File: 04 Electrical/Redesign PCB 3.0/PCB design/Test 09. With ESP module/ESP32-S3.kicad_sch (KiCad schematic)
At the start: 5 parts, among them U1 ESP32-S3-WROOM-1-N8R2

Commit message: Routing PCB test 9
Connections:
- net WS2812_CTRL is gone; now on net TOF_XSHUT: U1.39 (GPIO1/TOUCH1/ADC1_CH0)
- net Disp_CS: now also U1.7 (GPIO7/TOUCH7/ADC1_CH6); no longer U1.15 (GPIO3/TOUCH3/ADC1_CH2)
- net Disp_DC: now also U1.9 (GPIO16/U0CTS/ADC2_CH5/XTAL_32K_N); no longer U1.8 (GPIO15/U0RTS/ADC2_CH4/XTAL_32K_P)
- net Disp_LED: now also U1.15 (GPIO3/TOUCH3/ADC1_CH2); no longer U1.11 (GPIO18/U1RXD/ADC2_CH7/CLK_OUT3)
- net Disp_MISO: now also U1.21 (GPIO13/TOUCH13/ADC2_CH2/FSPIQ/FSPIIO7/SUBSPIQ); no longer U1.16 (GPIO46)
- net Disp_MOSI: now also U1.19 (GPIO11/TOUCH11/ADC2_CH0/FSPID/FSPIIO5/SUBSPID); no longer U1.18 (GPIO10/TOUCH10/ADC1_CH9/FSPICS0/FSPIIO4/SUBSPICS0)
- net Disp_RES: now also U1.8 (GPIO15/U0RTS/ADC2_CH4/XTAL_32K_P); no longer U1.7 (GPIO7/TOUCH7/ADC1_CH6)
- net Disp_SCK: now also U1.20 (GPIO12/TOUCH12/ADC2_CH1/FSPICLK/FSPIIO6/SUBSPICLK); no longer U1.17 (GPIO9/TOUCH9/ADC1_CH8/FSPIHD/SUBSPIHD)
- net SD_CS: now also U1.29 (SPIIO7/GPIO36/FSPICLK/SUBSPICLK); no longer U1.32 (MTCK/GPIO39/CLK_OUT3/SUBSPICS1)
- net SD_MISO: now also U1.31 (GPIO38/FSPIWP/SUBSPIWP); no longer U1.34 (MTDI/GPIO41/CLK_OUT1)
- net SD_MOSI: now also U1.30 (SPIDQS/GPIO37/FSPIQ/SUBSPIQ); no longer U1.33 (MTDO/GPIO40/CLK_OUT2)
- net SD_SCK: now also U1.32 (MTCK/GPIO39/CLK_OUT3/SUBSPICS1); no longer U1.35 (MTMS/GPIO42)
- net TOF_GPIO01: now also U1.38 (GPIO2/TOUCH2/ADC1_CH1); no longer U1.22 (GPIO14/TOUCH14/ADC2_CH3/FSPIWP/FSPIDQS/SUBSPIWP)
- net TOF_SCL: now also U1.37 (U0TXD/GPIO43/CLK_OUT1); no longer U1.20 (GPIO12/TOUCH12/ADC2_CH1/FSPICLK/FSPIIO6/SUBSPICLK)
- net TOF_SDA: now also U1.36 (U0RXD/GPIO44/CLK_OUT2); no longer U1.23 (GPIO21)
- net TOF_XSHUT: no longer U1.21 (GPIO13/TOUCH13/ADC2_CH2/FSPIQ/FSPIIO7/SUBSPIQ)
- net btn_back: now also U1.27 (GPIO0/BOOT); no longer U1.30 (SPIDQS/GPIO37/FSPIQ/SUBSPIQ)
- net btn_confirm: now also U1.28 (SPIIO6/GPIO35/FSPID/SUBSPID); no longer U1.31 (GPIO38/FSPIWP/SUBSPIWP)
- net btn_down: now also U1.33 (MTDO/GPIO40/CLK_OUT2); no longer U1.36 (U0RXD/GPIO44/CLK_OUT2)
- net btn_home: now also U1.35 (MTMS/GPIO42); no longer U1.38 (GPIO2/TOUCH2/ADC1_CH1)
- net btn_up: now also U1.34 (MTDI/GPIO41/CLK_OUT1); no longer U1.37 (U0TXD/GPIO43/CLK_OUT1)
- no-connect marks 10 -> 11

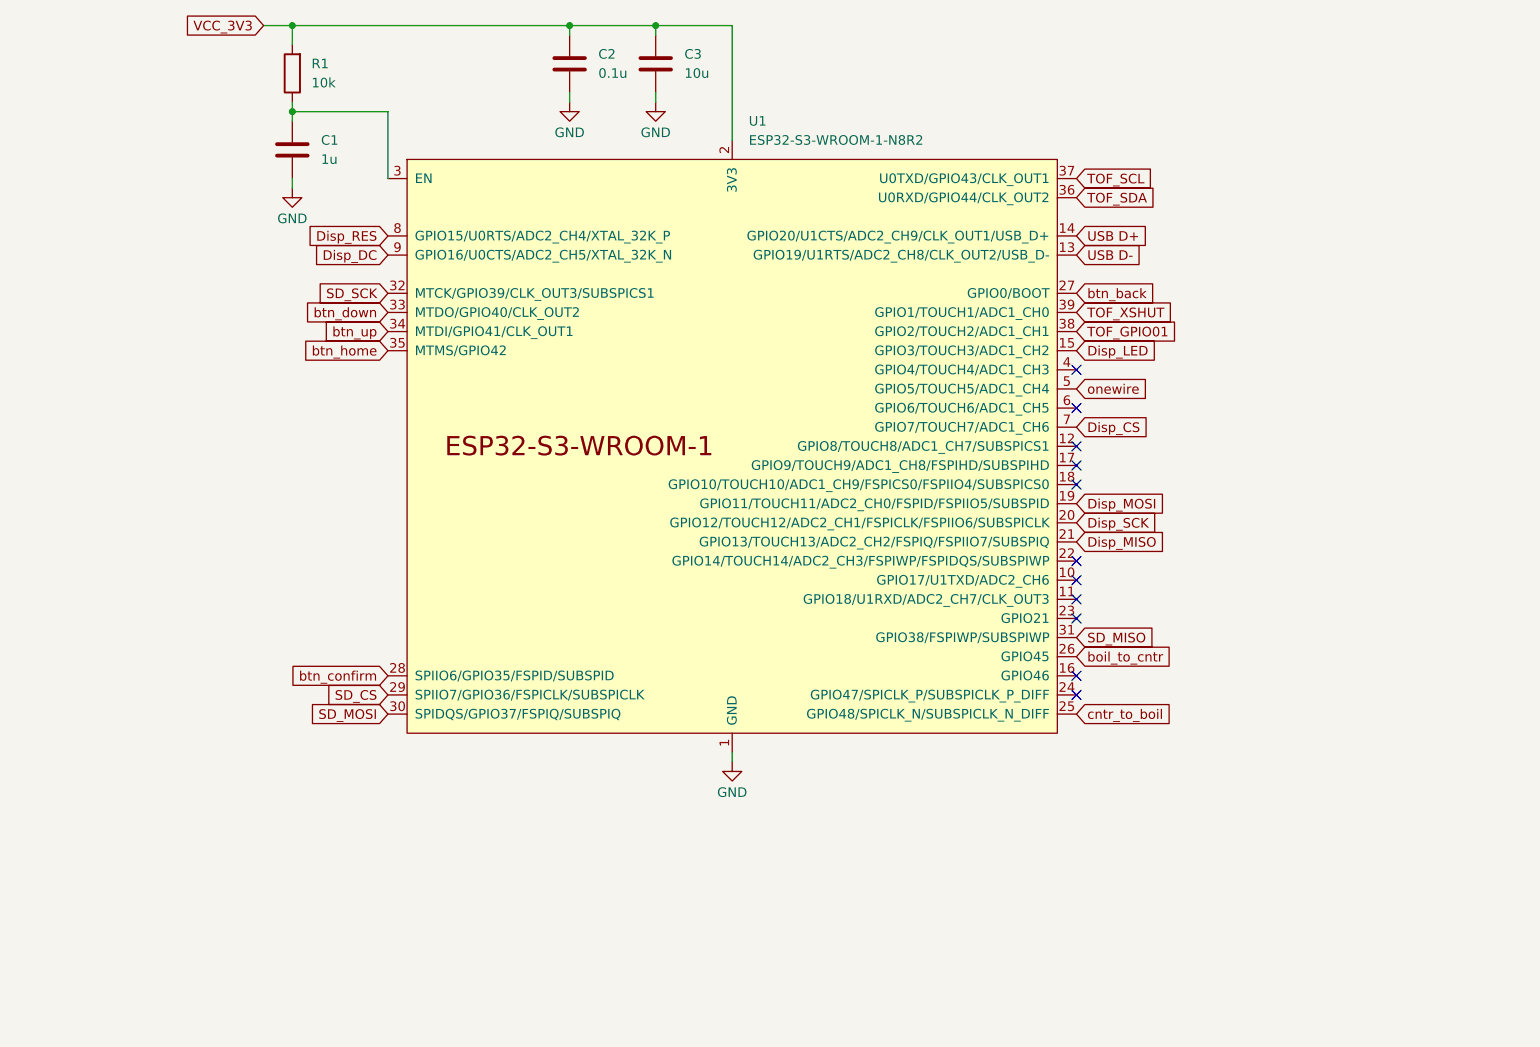
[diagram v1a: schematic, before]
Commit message: Logo added to PCB
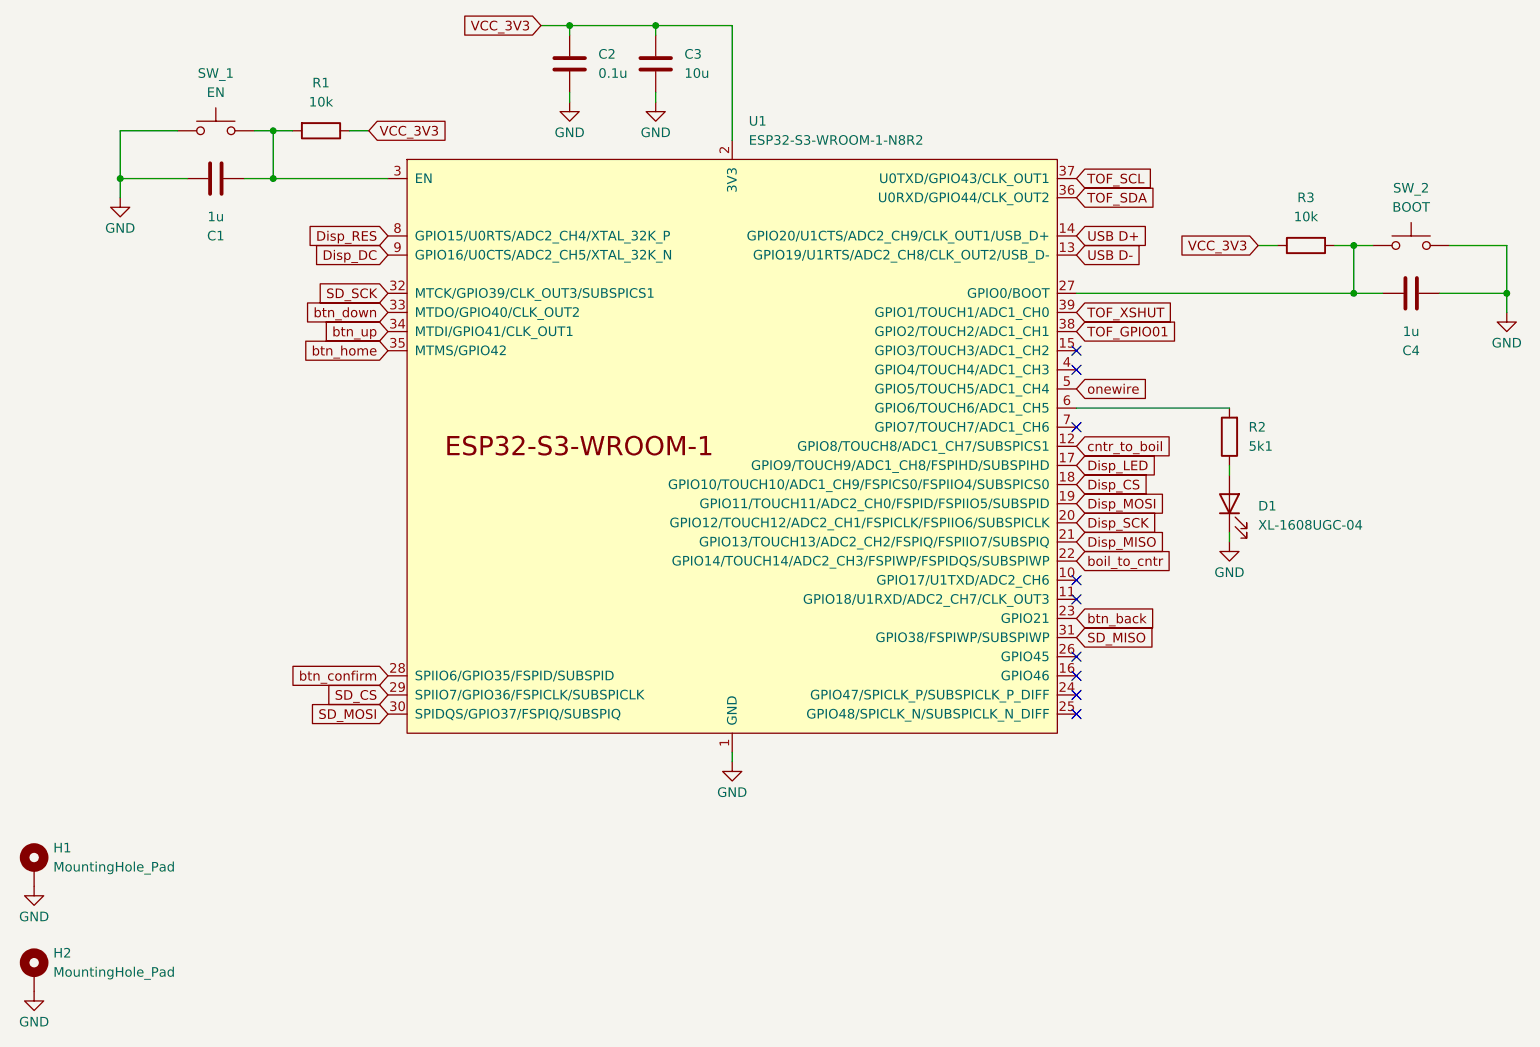
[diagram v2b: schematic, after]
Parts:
- added C4: 1u, Capacitor_SMD:C_0603_1608Metric, symbol Device:C
- added D1: XL-1608UGC-04, LED_SMD:LED_0603_1608Metric, symbol Device:LED
- added H1, H2: MountingHole_Pad, MountingHole:MountingHole_3.2mm_M3_ISO7380_Pad_TopBottom, symbol Mechanical:MountingHole_Pad
- added R2: 5k1, Resistor_SMD:R_0603_1608Metric, symbol Device:R
- added R3: 10k, Resistor_SMD:R_0603_1608Metric, symbol Device:R
- added SW_1: EN, Button_Switch_SMD:SW_SPST_TL3342, symbol Switch:SW_Push
- added SW_2: BOOT, Button_Switch_SMD:SW_SPST_TL3342, symbol Switch:SW_Push
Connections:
- net Disp_CS: now also U1.18 (GPIO10/TOUCH10/ADC1_CH9/FSPICS0/FSPIIO4/SUBSPICS0); no longer U1.7 (GPIO7/TOUCH7/ADC1_CH6)
- net Disp_LED: now also U1.17 (GPIO9/TOUCH9/ADC1_CH8/FSPIHD/SUBSPIHD); no longer U1.15 (GPIO3/TOUCH3/ADC1_CH2)
- net GND: now also C4.2, D1.1 (K), H1.1, H2.1, SW_1.2, SW_2.2
- net VCC_3V3: now also R1.1, R3.1; no longer R1.2
- net boil_to_cntr: now also U1.22 (GPIO14/TOUCH14/ADC2_CH3/FSPIWP/FSPIDQS/SUBSPIWP); no longer U1.26 (GPIO45)
- net btn_back: now also U1.23 (GPIO21); no longer U1.27 (GPIO0/BOOT)
- net cntr_to_boil: now also U1.12 (GPIO8/TOUCH8/ADC1_CH7/SUBSPICS1); no longer U1.25 (GPIO48/SPICLK_N/SUBSPICLK_N_DIFF)
- net at C1.1, U1.3 (EN): now also R1.2, SW_1.1; no longer R1.1
- net at U1.6 (GPIO6/TOUCH6/ADC1_CH5): now also R2.2
- new net: C4.1, R3.2, SW_2.1, U1.27 (GPIO0/BOOT)
- new net: D1.2 (A), R2.1
- no-connect marks 11 -> 9

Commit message: As ordered at JLCPCB
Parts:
- C3: LCSC Part #  C15525 -> C15525
- H1, H2: now not fitted
- SW_1, SW_2: LCSC C318884 -> (none); LCSC Part #  (none) -> C318884
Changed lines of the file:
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@@
 		(on_board yes)
 		(dnp no)
-		(property "Reference" "#PWR03"
+		(property "Reference" "#PWR05"
 			(at 140.97 57.15 0)
 			(effects
@@
 			(project "Test 09. With ESP module"
 				(path "/dee7d3c3-6abb-4cb3-8df4-3e3e37989a04/bd5268ae-2faf-441e-9d8c-8a98dae2e504"
-					(reference "#PWR03")
+					(reference "#PWR05")
 					(unit 1)
 				)
@@
 			)
 		)
+		(property "Comment" ""
+			(at 151.13 96.52 0)
+			(effects
+				(font
+					(size 1.27 1.27)
+				)
+				(hide yes)
+			)
+		)
 		(pin "16"
 		)
@@
 			)
 		)
-		(property "LCSC" "C318884"
+		(property "Comment" ""
+			(at 241.3 69.85 0)
+			(effects
+				(font
+					(size 1.27 1.27)
+				)
+				(hide yes)
+			)
+		)
+		(property "LCSC Part # " "C318884"
 			(at 241.3 69.85 0)
 			(effects
@@
 			)
 		)
-		(property "Datasheet" "~"
+		(property "Datasheet" "https://www.lcsc.com/datasheet/lcsc_datasheet_2206010045_UNI-ROYAL-Uniroyal-Elec-0603WAF1002T5E_C25804.pdf"
 			(at 227.33 69.85 0)
 			(effects
@@
 			)
 		)
-		(property "Description" "Resistor"
-			(at 227.33 69.85 0)
-			(effects
-				(font
-					(size 1.27 1.27)
-				)
-				(hide yes)
-			)
-		)
-		(property "Field7" ""
+		(property "Description" "100mW Thick Film Resistors 75V ±100ppm/℃ ±1% 10kΩ 0603 Chip Resistor - Surface Mount ROHS"
 			(at 227.33 69.85 0)
 			(effects
@@
 			)
 		)
+		(property "Comment" ""
+			(at 227.33 69.85 0)
+			(effects
+				(font
+					(size 1.27 1.27)
+				)
+				(hide yes)
+			)
+		)
 		(pin "2"
 		)
@@
 		(in_bom no)
 		(on_board yes)
-		(dnp no)
+		(dnp yes)
 		(fields_autoplaced yes)
 		(property "Reference" "H2"
@@
 			)
 		)
+		(property "Comment" ""
+			(at 58.42 166.37 0)
+			(effects
+				(font
+					(size 1.27 1.27)
+				)
+				(hide yes)
+			)
+		)
 		(pin "1"
 		)
@@
 		(on_board yes)
 		(dnp no)
-		(property "Reference" "#PWR06"
+		(property "Reference" "#PWR08"
 			(at 254 85.09 0)
 			(effects
@@
 			(project "Test 09. With ESP module"
 				(path "/dee7d3c3-6abb-4cb3-8df4-3e3e37989a04/bd5268ae-2faf-441e-9d8c-8a98dae2e504"
-					(reference "#PWR06")
+					(reference "#PWR08")
 					(unit 1)
 				)
@@
 			)
 		)
-		(property "Datasheet" "~"
+		(property "Datasheet" "https://www.lcsc.com/datasheet/lcsc_datasheet_2208231630_Samsung-Electro-Mechanics-CL05A106MQ5NUNC_C15525.pdf"
 			(at 140.97 45.72 0)
 			(effects
@@
 			)
 		)
-		(property "Description" "Unpolarized capacitor"
+		(property "Description" "6.3V 10uF X5R ±20% 0402 Multilayer Ceramic Capacitors MLCC - SMD/SMT ROHS"
 			(at 140.97 45.72 0)
 			(effects
@@
 			)
 		)
-		(property "Field7" ""
+		(property "LCSC Part # " "C15525"
 			(at 140.97 45.72 0)
 			(effects
@@
 			)
 		)
-		(property "LCSC Part # " " C15525"
+		(property "Comment" ""
 			(at 140.97 45.72 0)
 			(effects
@@
 			)
 		)
+		(property "Comment" ""
+			(at 217.17 104.14 0)
+			(effects
+				(font
+					(size 1.27 1.27)
+				)
+				(hide yes)
+			)
+		)
 		(pin "1"
 		)
@@
 			)
 		)
-		(property "Description" "Resistor"
+		(property "Description" "100mW Thick Film Resistors 75V ±100ppm/℃ ±1% 5.1kΩ 0603 Chip Resistor - Surface Mount ROHS"
 			(at 217.17 95.25 0)
 			(effects
@@
 		)
 		(property "LCSC Part # " "C23186"
+			(at 217.17 95.25 0)
+			(effects
+				(font
+					(size 1.27 1.27)
+				)
+				(hide yes)
+			)
+		)
+		(property "Comment" ""
 			(at 217.17 95.25 0)
 			(effects
@@
 			)
 		)
-		(property "Datasheet" "~"
+		(property "Datasheet" "https://www.lcsc.com/datasheet/lcsc_datasheet_2206010045_UNI-ROYAL-Uniroyal-Elec-0603WAF1002T5E_C25804.pdf"
 			(at 96.52 54.61 0)
 			(effects
@@
 			)
 		)
-		(property "Description" "Resistor"
+		(property "Description" "100mW Thick Film Resistors 75V ±100ppm/℃ ±1% 10kΩ 0603 Chip Resistor - Surface Mount ROHS"
 			(at 96.52 54.61 0)
 			(effects
@@
 			)
 		)
-		(property "Field7" ""
+		(property "LCSC Part # " "C25804"
 			(at 96.52 54.61 0)
 			(effects
@@
 			)
 		)
-		(property "LCSC Part # " "C25804"
+		(property "Comment" ""
 			(at 96.52 54.61 0)
 			(effects
@@
 		(on_board yes)
 		(dnp no)
-		(property "Reference" "#PWR01"
+		(property "Reference" "#PWR03"
 			(at 69.85 69.85 0)
 			(effects
@@
 			(project "Test 09. With ESP module"
 				(path "/dee7d3c3-6abb-4cb3-8df4-3e3e37989a04/bd5268ae-2faf-441e-9d8c-8a98dae2e504"
-					(reference "#PWR01")
+					(reference "#PWR03")
 					(unit 1)
 				)
@@
 		(on_board yes)
 		(dnp no)
-		(property "Reference" "#PWR04"
+		(property "Reference" "#PWR06"
 			(at 151.13 144.78 0)
 			(effects
@@
 			(project "Test 09. With ESP module"
 				(path "/dee7d3c3-6abb-4cb3-8df4-3e3e37989a04/bd5268ae-2faf-441e-9d8c-8a98dae2e504"
-					(reference "#PWR04")
+					(reference "#PWR06")
 					(unit 1)
 				)
@@
 		(on_board yes)
 		(dnp no)
-		(property "Reference" "#PWR02"
+		(property "Reference" "#PWR04"
 			(at 129.54 57.15 0)
 			(effects
@@
 			(project "Test 09. With ESP module"
 				(path "/dee7d3c3-6abb-4cb3-8df4-3e3e37989a04/bd5268ae-2faf-441e-9d8c-8a98dae2e504"
-					(reference "#PWR02")
+					(reference "#PWR04")
 					(unit 1)
 				)
@@
 		(on_board yes)
 		(dnp no)
-		(property "Reference" "#PWR038"
+		(property "Reference" "#PWR02"
 			(at 58.42 175.26 0)
 			(effects
@@
 			(project "Test 09. With ESP module"
 				(path "/dee7d3c3-6abb-4cb3-8df4-3e3e37989a04/bd5268ae-2faf-441e-9d8c-8a98dae2e504"
-					(reference "#PWR038")
+					(reference "#PWR02")
 					(unit 1)
 				)
@@
 			)
 		)
-		(property "Datasheet" "~"
+		(property "Datasheet" "https://www.lcsc.com/datasheet/lcsc_datasheet_2304140030_Samsung-Electro-Mechanics-CL10A105KB8NNNC_C15849.pdf"
 			(at 241.3 76.2 0)
 			(effects
@@
 			)
 		)
-		(property "Description" "Unpolarized capacitor"
-			(at 241.3 76.2 0)
-			(effects
-				(font
-					(size 1.27 1.27)
-				)
-				(hide yes)
-			)
-		)
-		(property "Field7" ""
+		(property "Description" "50V 1uF X5R ±10% 0603 Multilayer Ceramic Capacitors MLCC - SMD/SMT ROHS"
 			(at 241.3 76.2 0)
 			(effects
@@
 			)
 		)
+		(property "Comment" ""
+			(at 241.3 76.2 0)
+			(effects
+				(font
+					(size 1.27 1.27)
+				)
+				(hide yes)
+			)
+		)
 		(pin "2"
 		)
@@
 		(on_board yes)
 		(dnp no)
-		(property "Reference" "#PWR037"
+		(property "Reference" "#PWR01"
 			(at 58.42 161.29 0)
 			(effects
@@
 			(project "Test 09. With ESP module"
 				(path "/dee7d3c3-6abb-4cb3-8df4-3e3e37989a04/bd5268ae-2faf-441e-9d8c-8a98dae2e504"
-					(reference "#PWR037")
+					(reference "#PWR01")
 					(unit 1)
 				)
@@
 			)
 		)
-		(property "Datasheet" "~"
+		(property "Datasheet" "https://www.lcsc.com/datasheet/lcsc_datasheet_2304140030_Samsung-Electro-Mechanics-CL10A105KB8NNNC_C15849.pdf"
 			(at 82.55 60.96 0)
 			(effects
@@
 			)
 		)
-		(property "Description" "Unpolarized capacitor"
-			(at 82.55 60.96 0)
-			(effects
-				(font
-					(size 1.27 1.27)
-				)
-				(hide yes)
-			)
-		)
-		(property "Field7" ""
+		(property "Description" "50V 1uF X5R ±10% 0603 Multilayer Ceramic Capacitors MLCC - SMD/SMT ROHS"
 			(at 82.55 60.96 0)
 			(effects
@@
 			)
 		)
+		(property "Comment" ""
+			(at 82.55 60.96 0)
+			(effects
+				(font
+					(size 1.27 1.27)
+				)
+				(hide yes)
+			)
+		)
 		(pin "2"
 		)
@@
 		(on_board yes)
 		(dnp no)
-		(property "Reference" "#PWR05"
+		(property "Reference" "#PWR07"
 			(at 217.17 115.57 0)
 			(effects
@@
 			(project "Test 09. With ESP module"
 				(path "/dee7d3c3-6abb-4cb3-8df4-3e3e37989a04/bd5268ae-2faf-441e-9d8c-8a98dae2e504"
-					(reference "#PWR05")
+					(reference "#PWR07")
 					(unit 1)
 				)
@@
 			)
 		)
-		(property "Datasheet" "~"
+		(property "Datasheet" "https://www.lcsc.com/datasheet/lcsc_datasheet_2211101700_YAGEO-CC0603KRX7R9BB104_C14663.pdf"
 			(at 129.54 45.72 0)
 			(effects
@@
 			)
 		)
-		(property "Description" "Unpolarized capacitor"
+		(property "Description" "50V 100nF X7R ±10% 0603 Multilayer Ceramic Capacitors MLCC - SMD/SMT ROHS"
 			(at 129.54 45.72 0)
 			(effects
@@
 			)
 		)
-		(property "Field7" ""
+		(property "LCSC Part # " "C14663"
 			(at 129.54 45.72 0)
 			(effects
@@
 			)
 		)
-		(property "LCSC Part # " "C14663"
+		(property "Comment" ""
 			(at 129.54 45.72 0)
 			(effects
@@
 			)
 		)
-		(property "LCSC" "C318884"
+		(property "Comment" ""
+			(at 82.55 54.61 0)
+			(effects
+				(font
+					(size 1.27 1.27)
+				)
+				(hide yes)
+			)
+		)
+		(property "LCSC Part # " "C318884"
 			(at 82.55 54.61 0)
 			(effects
@@
 		(in_bom no)
 		(on_board yes)
-		(dnp no)
+		(dnp yes)
 		(fields_autoplaced yes)
 		(property "Reference" "H1"
@@
 			(at 58.42 152.4 0)
 			(effects
+				(font
+					(size 1.27 1.27)
+				)
+				(hide yes)
+			)
+		)
+		(property "Comment" ""
+			(at 58.42 152.4 0)
+			(effects
